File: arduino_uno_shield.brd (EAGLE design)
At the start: 53 x 59.7 mm, 14 parts

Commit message: save
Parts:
- moved R3 6.35 mm to (24.1, 21.6), turned to 90 degrees
- moved LED1 4.02 mm to (16.5, 21.6)
- moved POT1 1.27 mm to (17.8, 41.9)
- moved POT2 1.27 mm to (17.8, 36.8)
- moved POT3 1.27 mm to (17.8, 31.8)
- moved C2 1.27 mm to (30.5, 6.35)
- moved MIC 1.27 mm to (17.8, 47.0)
- renumbered MCP3208 to ADC, MCP4921 to DAC
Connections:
- net N$1 renamed AUD
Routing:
- net GND: track 0.00 -> 160.0 mm
- net N$4: track 0.00 -> 84.3 mm
- net 3.3V: track 0.00 -> 71.8 mm
- net N$7: track 0.00 -> 61.0 mm
- net N$5: track 0.00 -> 58.2 mm
- net N$6: track 0.00 -> 55.8 mm
- net N$11: track 0.00 -> 45.7 mm
- net 5V: track 0.00 -> 43.6 mm
- net N$13: track 0.00 -> 42.5 mm
- net N$3: track 0.00 -> 36.3 mm
- net N$12: track 0.00 -> 26.8 mm
- net N$9: track 0.00 -> 23.3 mm
- net N$15: track 0.00 -> 21.0 mm
- net N$8: track 0.00 -> 18.2 mm
- net N$14: track 0.00 -> 17.7 mm
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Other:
- board text added: "3V"
- board text added: "GND"
- board text added: "SIG"

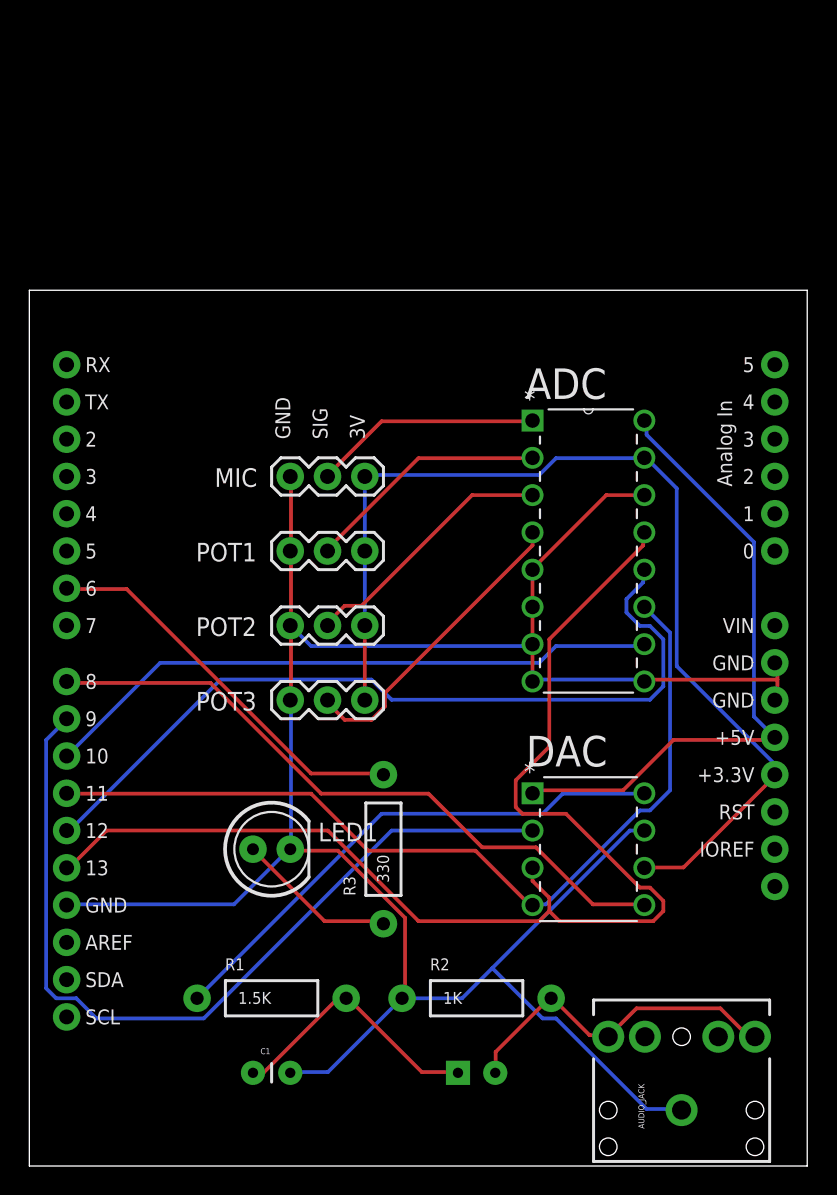
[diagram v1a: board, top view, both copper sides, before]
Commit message: clean up board layout
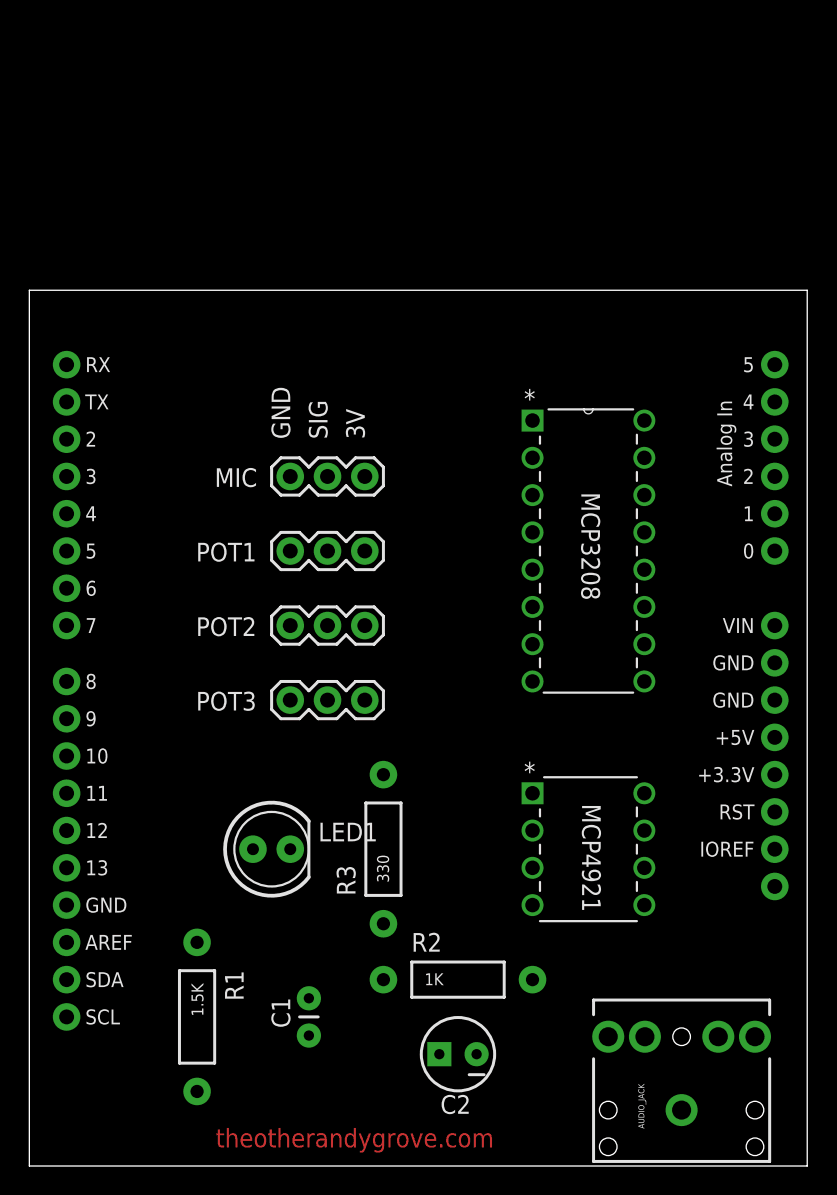
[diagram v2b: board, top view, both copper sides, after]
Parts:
- moved R1 5.24 mm to (11.4, 10.2), turned to 270 degrees
- moved C1 4.58 mm to (19.1, 8.89), turned to 90 degrees
- moved C2 1.80 mm to (29.2, 7.62), flipped to the top, turned to 180 degrees
- moved R2 1.80 mm to (29.2, 12.7)
- renumbered ADC to MCP3208, DAC to MCP4921
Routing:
- net GND: track 160.0 -> 0.00 mm
- net N$4: track 84.3 -> 0.00 mm
- net 3.3V: track 71.8 -> 0.00 mm
- net N$7: track 61.0 -> 0.00 mm
- net N$5: track 58.2 -> 0.00 mm
- net N$6: track 55.8 -> 0.00 mm
- net N$11: track 45.7 -> 0.00 mm
- net 5V: track 43.6 -> 0.00 mm
- net N$13: track 42.5 -> 0.00 mm
- net N$3: track 36.3 -> 0.00 mm
- net N$12: track 26.8 -> 0.00 mm
- net N$9: track 23.3 -> 0.00 mm
- net N$15: track 21.0 -> 0.00 mm
- net N$8: track 18.2 -> 0.00 mm
- net N$14: track 17.7 -> 0.00 mm
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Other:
- board text added: "theotherandygrove.com"

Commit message: add more pot headers
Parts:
- removed LED1: (no value), SparkFun-LED:LED5MM
- added LED: (no value), SparkFun-LED:LED5MM
- added POT4, POT5, POT6, POT7: (no value), SparkFun-Connectors:1X03
- moved R1 28.2 mm to (27.9, 33.0)
- moved R3 15.9 mm to (16.5, 7.62), turned to 180 degrees
- moved C1 15.5 mm to (27.9, 21.6)
- moved R2 14.5 mm to (43.2, 16.5)
- moved C2 9.67 mm to (33.0, 16.5)
- moved MCP4921 7.73 mm to (43.2, 25.4)
- moved MCP3208 5.24 mm to (43.2, 38.1)
- moved POT1 4.02 mm to (14.0, 43.2)
- moved POT2 4.02 mm to (14.0, 38.1)
- moved POT3 4.02 mm to (14.0, 33.0)
- moved MIC 4.02 mm to (14.0, 48.3)
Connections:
- new net N$1: MCP3208.5, POT4.2
- new net N$16: MCP3208.6, POT5.2
- new net N$17: MCP3208.7, POT6.2
- new net N$18: MCP3208.8, POT7.2
- net 3.3V: now also POT4.3, POT5.3, POT6.3, POT7.3
- net GND: now also LED.K, POT4.1, POT5.1, POT6.1, POT7.1; no longer LED1.K, MCP3208.5, MCP3208.6, MCP3208.7, MCP3208.8
- net N$10: now also LED.A; no longer LED1.A
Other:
- board text removed: "theotherandygrove.com"

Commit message: created board from scratch
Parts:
- removed MIC, POT1, POT2, POT3, POT4, POT5, POT6, POT7: (no value), SparkFun-Connectors:1X03
- added A1, A2, A3, A4, A5, A6, A7, A8: (no value), SparkFun-Connectors:1X03
- added EXT_LED: M023.5MM, SparkFun-Connectors:SCREWTERMINAL-3.5MM-2
- moved MCP4921 27.9 mm to (19.1, 39.4)
- moved C2 26.9 mm to (41.9, 41.9)
- moved R2 26.9 mm to (34.3, 41.9), turned to 270 degrees
- moved R3 26.7 mm to (15.2, 34.3)
- moved LED 22.9 mm to (15.2, 26.7), turned to 90 degrees
- moved AUDIO_JACK 20.3 mm to (44.5, 24.1)
- moved U$1 20.3 mm to (0.00, 20.3)
- moved MCP3208 14.0 mm to (43.2, 52.1)
- moved C1 10.2 mm to (29.2, 31.8), turned to 0 degrees
- moved R1 8.98 mm to (26.7, 41.9)
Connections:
- net N$7 renamed A6
- net 3.3V: now also A1.3, A2.3, A3.3, A4.3, A5.3, A6.3, A7.3, A8.3; no longer MIC.3, POT1.3, POT2.3, POT3.3, POT4.3, POT5.3, POT6.3, POT7.3
- net AUD: now also A1.2; no longer MIC.2
- net GND: now also A1.1, A2.1, A3.1, A4.1, A5.1, A6.1, A7.1, A8.1, EXT_LED.1; no longer MIC.1, POT1.1, POT2.1, POT3.1, POT4.1, POT5.1, POT6.1, POT7.1
- net N$1: now also A5.2; no longer POT4.2
- net N$12: now also EXT_LED.2
- net N$14: now also A3.2; no longer POT2.2
- net N$15: now also A4.2; no longer POT3.2
- net N$16: now also A6.2; no longer POT5.2
- net N$17: now also A7.2; no longer POT6.2
- net N$18: now also A8.2; no longer POT7.2
- net N$2: now also A2.2; no longer POT1.2
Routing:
- net GND: track 0.00 -> 177.1 mm
- net 3.3V: track 0.00 -> 100.1 mm
- net 5V: track 0.00 -> 78.7 mm
- net A6: track 0.00 -> 63.8 mm
- net N$12: track 0.00 -> 61.4 mm
- net N$4: track 0.00 -> 59.7 mm
- net N$6: track 0.00 -> 54.2 mm
- net N$13: track 0.00 -> 43.3 mm
- net N$9: track 0.00 -> 30.5 mm
- net N$15: track 0.00 -> 24.0 mm
- net N$14: track 0.00 -> 22.9 mm
- net N$8: track 0.00 -> 22.4 mm
- net N$11: track 0.00 -> 22.3 mm
- net N$2: track 0.00 -> 21.9 mm
- net AUD: track 0.00 -> 20.9 mm
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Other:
- board size 53 x 59.7 mm -> 53 x 57.1 mm
- board text added: "IN"
- board text removed: "SIG"

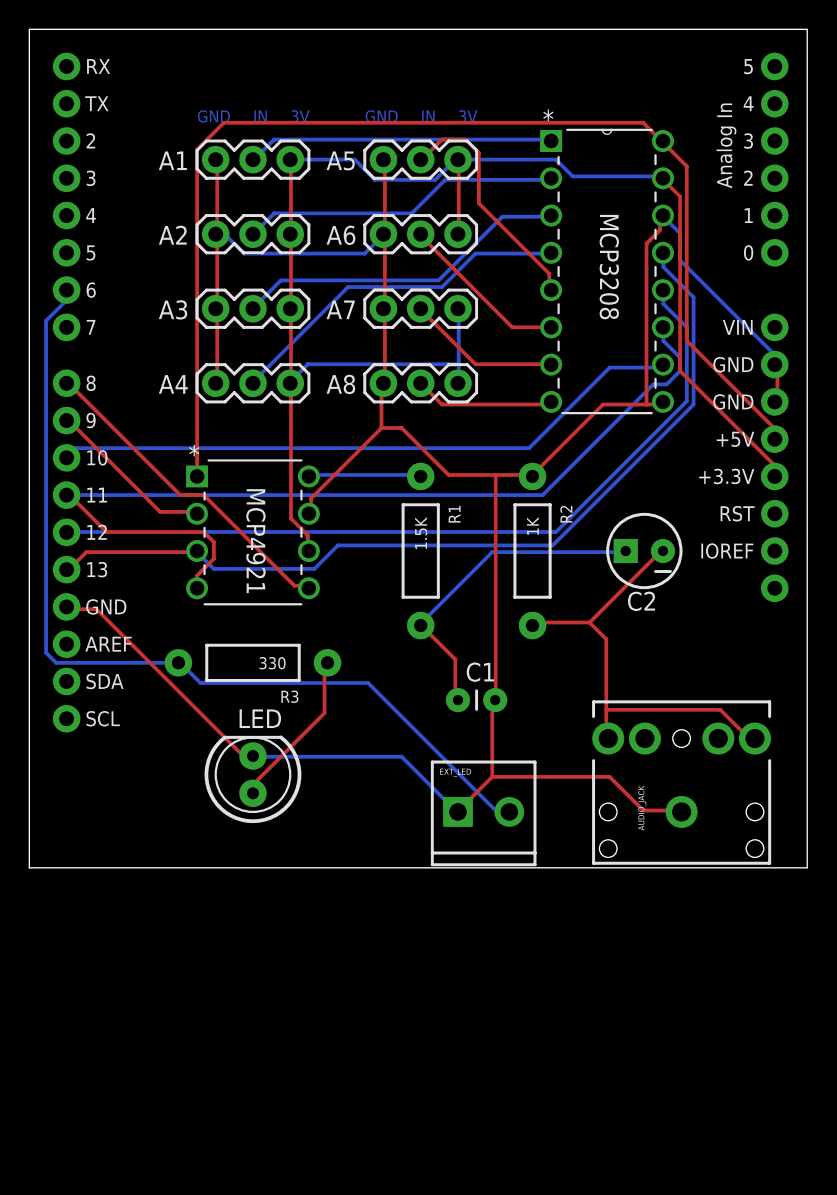
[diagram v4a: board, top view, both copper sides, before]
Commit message: fixed polarity issue on LED screw terminal
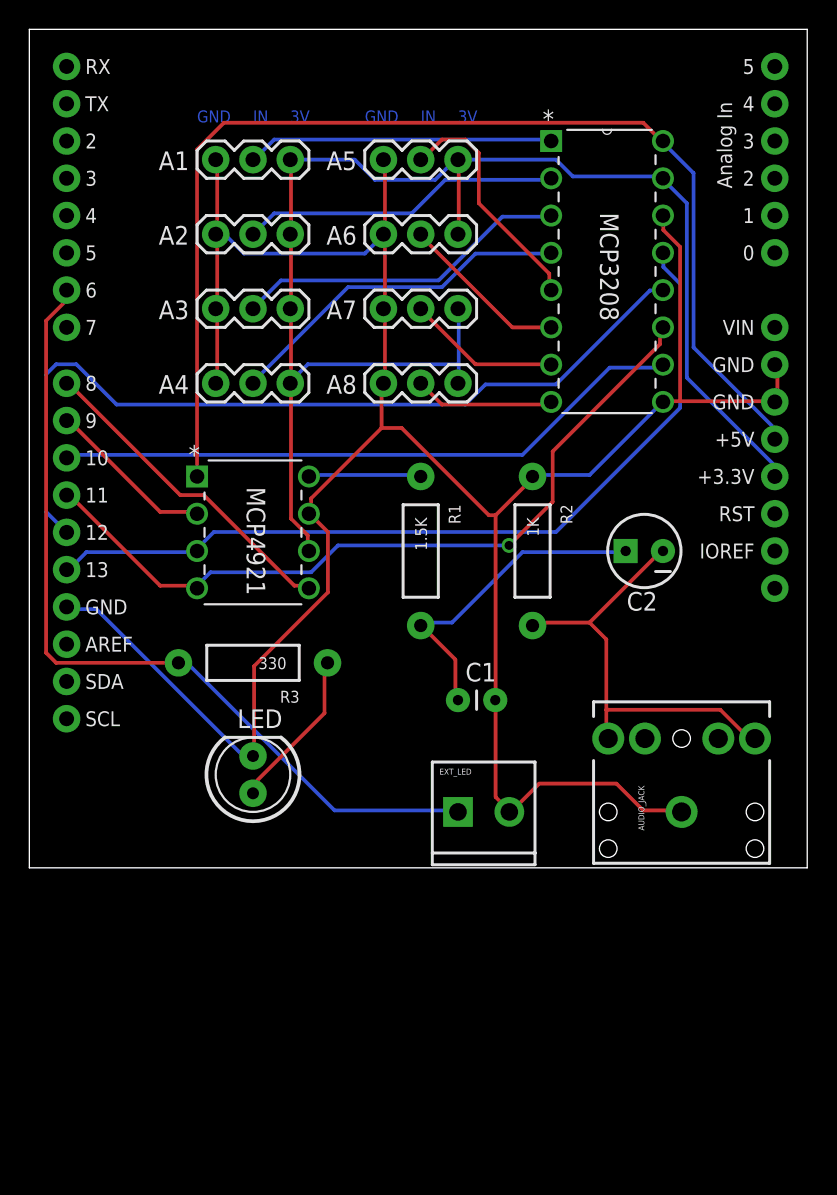
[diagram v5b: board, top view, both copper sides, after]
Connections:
- net GND: now also EXT_LED.2; no longer EXT_LED.1
- net N$12: now also EXT_LED.1; no longer EXT_LED.2
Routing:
- net A6: track 63.8 -> 53.5 mm, vias 0 -> 1
- net GND: track 177.1 -> 173.2 mm
- net N$6: track 54.2 -> 58.0 mm
- net N$12: track 61.4 -> 57.8 mm
- net N$4: track 59.7 -> 57.5 mm

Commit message: save latest
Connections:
- net A6 renamed SPI_MOSI
- net N$13 renamed CS_ADC
- net N$4 renamed SPI_CLK
- net N$5 renamed CS_DAC
- net N$6 renamed SPI_MISO
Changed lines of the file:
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@@
 <wire x1="49.3776" y1="29.2608" x2="49.45" y2="29.13" width="0.254" layer="1"/>
 </signal>
-<signal name="N$4">
+<signal name="SPI_CLK">
 <contactref element="U$1" pad="D13"/>
 <contactref element="MCP3208" pad="13"/>
@@
 <wire x1="15.3162" y1="63.5508" x2="15.24" y2="63.5" width="0.254" layer="16"/>
 </signal>
-<signal name="N$6">
+<signal name="SPI_MISO">
 <contactref element="U$1" pad="D12"/>
 <contactref element="MCP3208" pad="12"/>
@@
 <wire x1="42.9768" y1="59.6646" x2="43.18" y2="59.69" width="0.254" layer="16"/>
 </signal>
-<signal name="A6">
+<signal name="SPI_MOSI">
+<contactref element="MCP4921" pad="4"/>
 <contactref element="U$1" pad="D11"/>
 <contactref element="MCP3208" pad="11"/>
-<contactref element="MCP4921" pad="4"/>
 <wire x1="8.9154" y1="39.5478" x2="11.43" y2="39.5478" width="0.254" layer="1"/>
 <wire x1="2.7432" y1="45.72" x2="8.9154" y2="39.5478" width="0.254" layer="1"/>
@@
 <wire x1="2.7432" y1="53.2638" x2="2.54" y2="53.34" width="0.254" layer="1"/>
 </signal>
-<signal name="N$13">
+<signal name="CS_ADC">
 <contactref element="MCP3208" pad="10"/>
 <contactref element="U$1" pad="D10"/>
@@
 <wire x1="2.7432" y1="48.4632" x2="2.54" y2="48.26" width="0.254" layer="16"/>
 </signal>
-<signal name="N$5">
+<signal name="CS_DAC">
 <contactref element="MCP4921" pad="2"/>
 <contactref element="U$1" pad="D9"/>

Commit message: save
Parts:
- moved C1 10.2 mm to (29.2, 41.9), turned to 90 degrees
- moved R1 2.84 mm to (24.1, 43.2)
- moved C2 1.80 mm to (40.6, 43.2)
- moved LED 1.27 mm to (15.2, 25.4)
- moved R2 1.27 mm to (34.3, 43.2)
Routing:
- net GND: track 173.2 -> 196.3 mm
- net SPI_MOSI: track 53.5 -> 60.4 mm, vias 1 -> 0
- net N$8: track 22.4 -> 17.4 mm
- net SPI_MISO: track 58.0 -> 54.3 mm
- net N$3: track 7.68 -> 5.59 mm
- net N$10: track 11.1 -> 12.4 mm
- net N$9: track 30.5 -> 31.0 mm

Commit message: save
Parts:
- added FRAME3: FRAME-LETTER, SparkFun-Aesthetics:CREATIVE_COMMONS
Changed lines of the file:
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@@
 <element name="C1" library="SparkFun-Passives" package="CAP-PTH-SMALL" value="0.1uF" x="29.21" y="41.91" smashed="yes" rot="R90">
 <attribute name="NAME" x="27.94" y="42.418" size="1.27" layer="25" rot="R90"/>
-<attribute name="VALUE" x="32.004" y="40.894" size="1.27" layer="27" rot="R90"/>
+<attribute name="VALUE" x="32.004" y="40.894" size="1.27" layer="21" rot="R90"/>
 </element>
 <element name="C2" library="SparkFun-Passives" package="CPOL-RADIAL-10UF-25V" value="10uF" x="40.64" y="43.18" smashed="yes" rot="R180">
 <attribute name="NAME" x="41.529" y="40.386" size="1.27" layer="25" rot="R180"/>
-<attribute name="VALUE" x="42.545" y="46.863" size="1.27" layer="27" rot="R180"/>
+<attribute name="VALUE" x="42.545" y="46.863" size="1.27" layer="21" rot="R180"/>
 </element>
 <element name="LED" library="SparkFun-LED" package="LED5MM" value="" x="15.24" y="25.4" smashed="yes" rot="R90">
@@
 <element name="U$1" library="SparkFun-Boards" package="UNO_R3_SHIELD" value="ARDUINO_R3_SHIELD" x="0" y="20.32"/>
 <element name="EXT_LED" library="SparkFun-Connectors" package="SCREWTERMINAL-3.5MM-2" value="M023.5MM" x="29.21" y="24.13"/>
+<element name="FRAME3" library="SparkFun-Aesthetics" package="CREATIVE_COMMONS" value="FRAME-LETTER" x="20.32" y="-21.59"/>
 </elements>
 <signals>
